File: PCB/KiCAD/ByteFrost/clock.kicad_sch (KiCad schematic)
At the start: 16 parts, among them SW101 Single_Step, SW102 Break, SW103 Cont., U101 ICM7555xB, U102 ICM7555xB, U103 74HC76

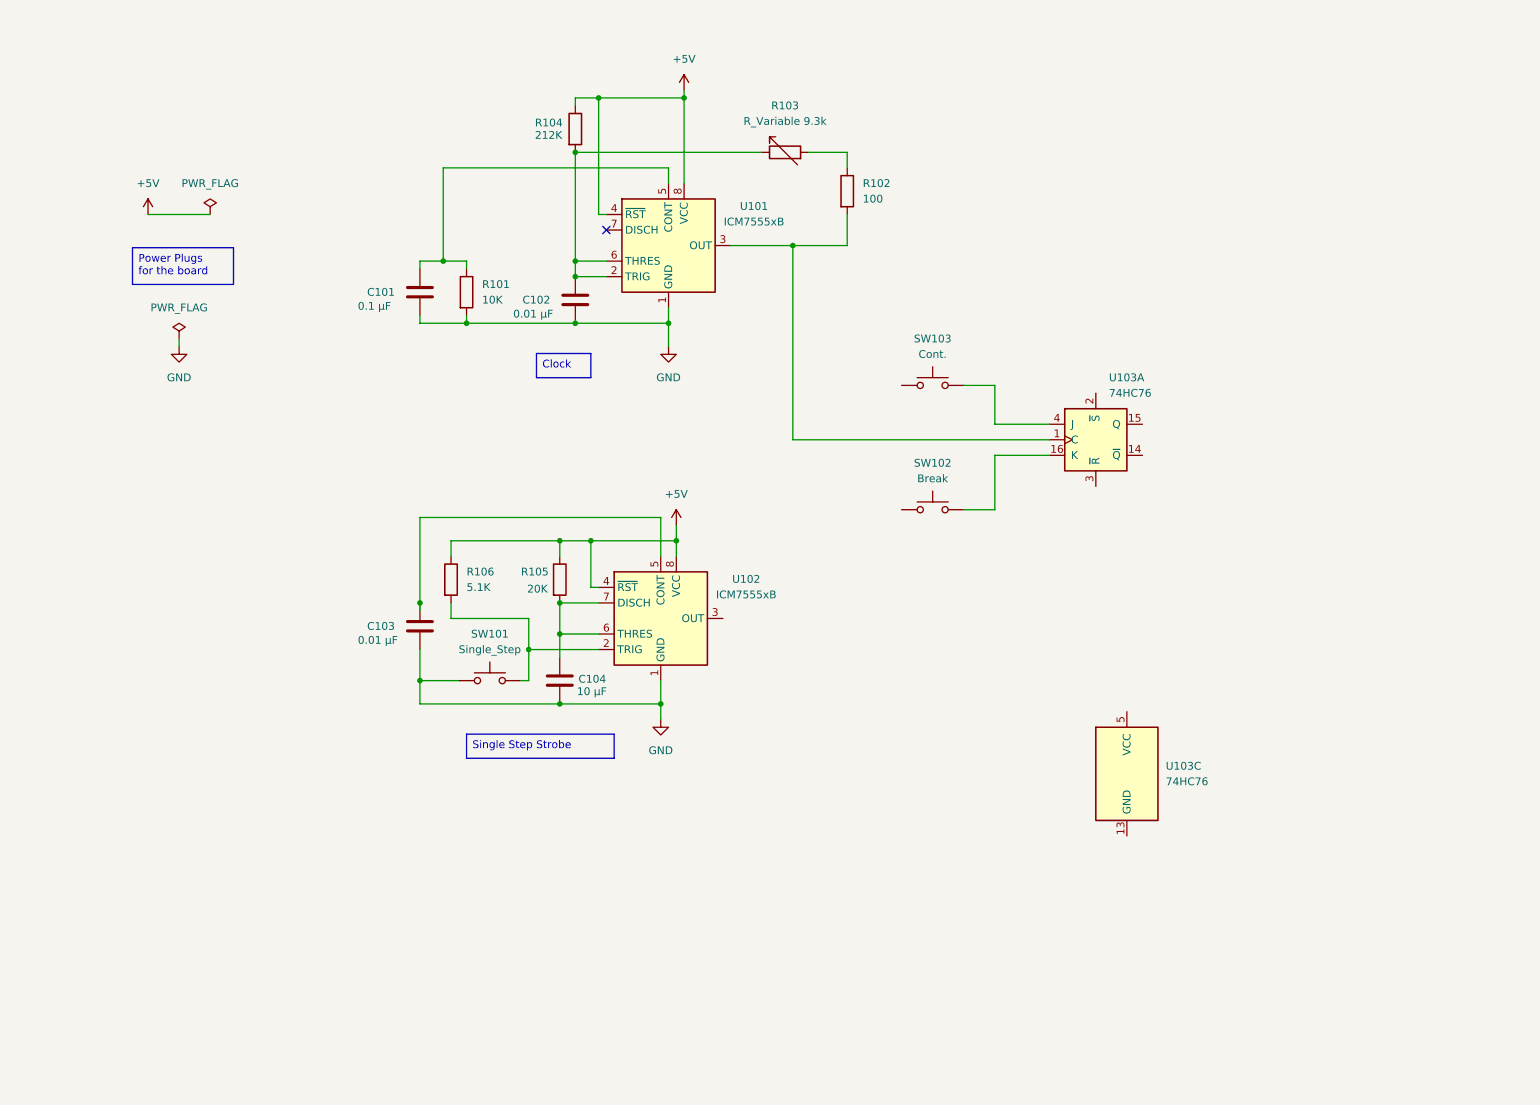
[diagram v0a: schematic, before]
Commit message: Finish KiCAD Clock and Reset
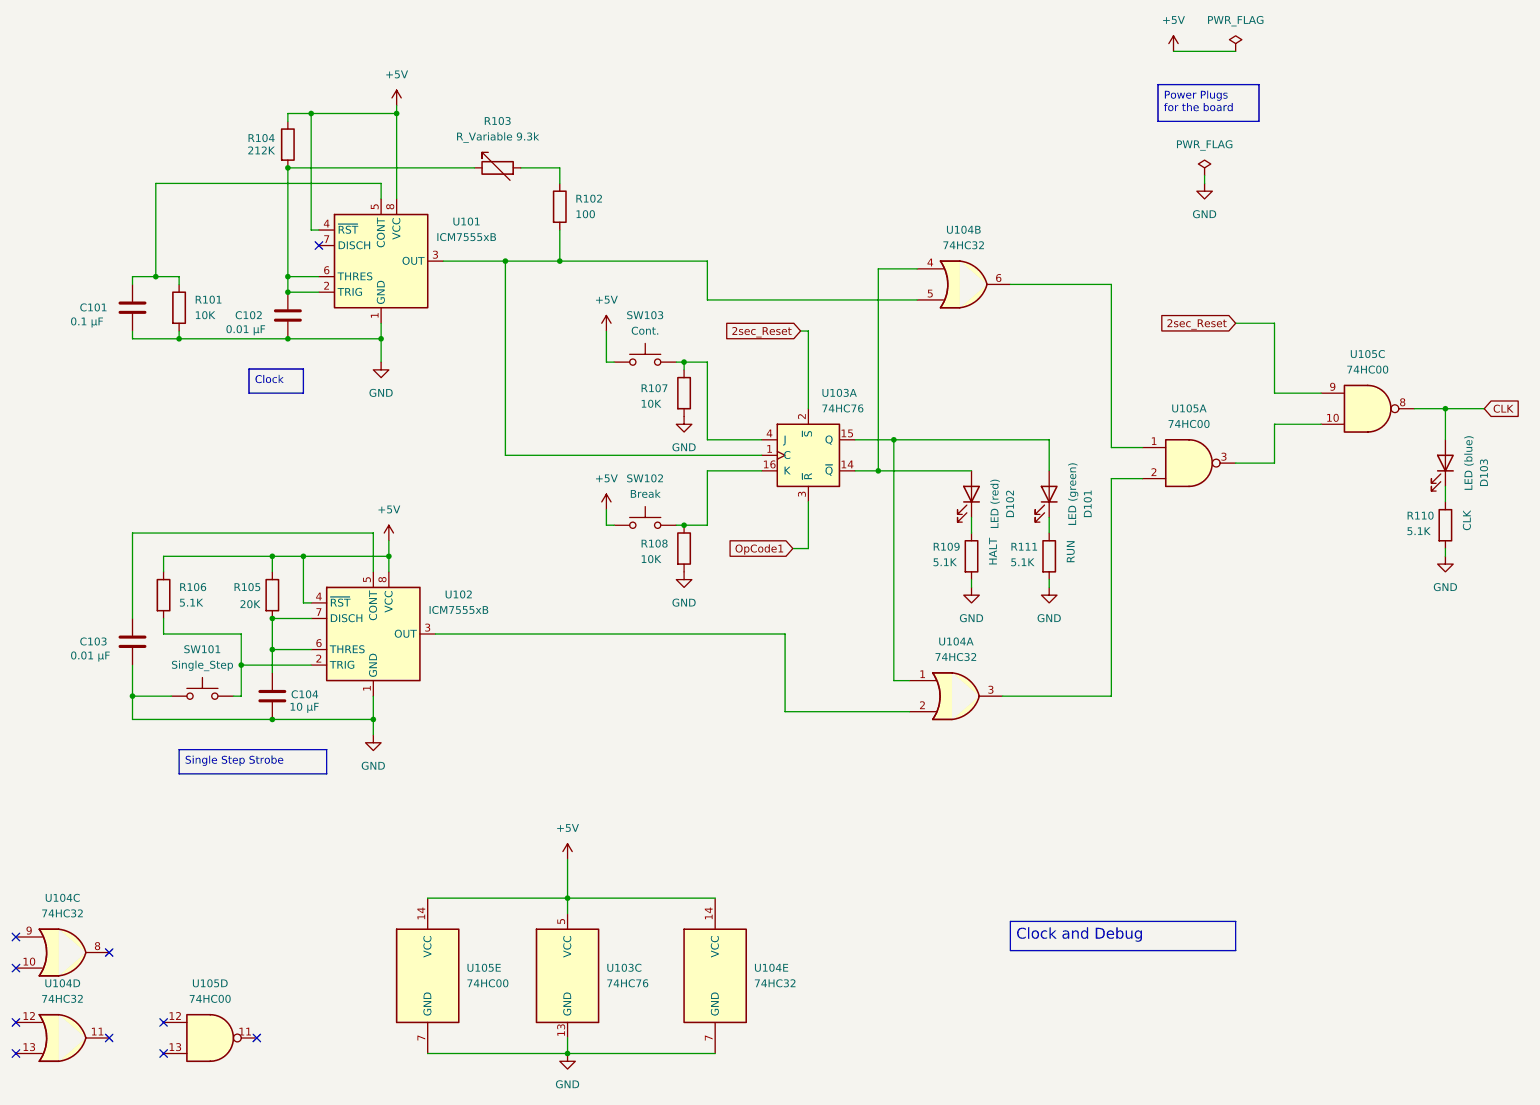
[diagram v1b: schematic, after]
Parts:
- added D101: LED (green), LED_THT:LED_D5.0mm, symbol Device:LED
- added D102: LED (red), LED_THT:LED_D5.0mm, symbol Device:LED
- added D103: LED (blue), LED_THT:LED_D5.0mm, symbol Device:LED
- added R107, R108: 10K, Resistor_THT:R_Axial_DIN0207_L6.3mm_D2.5mm_P10.16mm_Horizontal, symbol Device:R
- added R109, R110, R111: 5.1K, Resistor_THT:R_Axial_DIN0207_L6.3mm_D2.5mm_P10.16mm_Horizontal, symbol Device:R
- added U104: 74HC32, Package_DIP:DIP-14_W7.62mm_Socket, symbol 74xx:74LS32
- added U105: 74HC00, Package_DIP:DIP-14_W7.62mm_Socket, symbol 74xx:74HC00
- R101, R102, R104, R105, R106: footprint (none) -> Resistor_THT:R_Axial_DIN0207_L6.3mm_D2.5mm_P10.16mm_Horizontal
- SW101, SW102, SW103: footprint (none) -> Button_Switch_THT:SW_PUSH_6mm_H7.3mm
- U103: footprint (none) -> Package_DIP:DIP-16_W7.62mm_Socket
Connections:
- net +5V: now also SW102.1, SW103.1, U103.5 (VCC), U104.14 (VCC), U105.14 (VCC)
- net GND: now also U103.13 (GND), R107.2, R108.2, R109.2, R110.2, R111.2, U104.7 (GND), U105.7 (GND)
- net at R102.2, U101.3 (OUT), U103.1 (C): now also U104.5
- net at U103.14 (~{Q}): now also D102.2 (A), U104.4
- net at U103.15 (Q): now also D101.2 (A), U104.1
- net at SW102.2, U103.16 (K): now also R108.1
- net 2sec_Reset: now reaches U103.2 (~{S})
- net 2sec_Reset: now also U105.9
- net OpCode1: now reaches U103.3 (~{R})
- net at SW103.2, U103.4 (J): now also R107.1
- net at U102.3 (OUT): now also U104.2
- new net: U104.3, U105.2
- new net: D102.1 (K), R109.1
- new net: U105.10, U105.3
- new net: U104.6, U105.1
- new net: D103.1 (K), R110.1
- new net: D101.1 (K), R111.1
- new net CLK: D103.2 (A), U105.8
- no-connect marks 1 -> 10
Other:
- moved on the sheet: C101, C102, C103, C104, R101, R102, R103, R104, R105, R106, SW101, SW102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
